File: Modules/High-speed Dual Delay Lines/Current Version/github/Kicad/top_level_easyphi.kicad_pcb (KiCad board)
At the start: 4 copper layers, 265 parts, among them J1 JTAG_CONNEC, J2 DM3D-SF(AS), P1 CONN_8, Q1 MOS_P, Q2 FDD8780, Q3 FDD8780, U1 MAX5924D, U10 2-1825027-0, U11 RLP1-600-800, U12 TE-5650478-5, U13 MAX9032AKA, U14 NB4L52, U15 TROU_FIX, U16 TROU_FIX, U17 RLP1-600-800, U18 RLP1-600-800, U19 RLP1-600-800, U2 MAX5925D, U20 RLP1-600-800, U21 RLP1-600-800, U22 CONNEC_QMA_ANO_2622-4035, U23 RLP1-600-800, U24 CONNEC_QMA_ANO_2622-4035, U25 CONNEC_QMA_ANO_2622-4035, U26 CONNEC_QMA_ANO_2622-4035, U27 CONNEC_QMA_ANO_2622-4035, U28 CONNEC_QMA_ANO_2622-4035, U29 NB6L11M, U3 24LC64, U30 SY89851U, U31 SY89297U, U32 MAX9032AKA, U33 NB4L52, U34 SY89851U, U35 NB6L11M, U36 AOZ1280, U4 USBLC6-2, U5 TPS7A4901, U51 CARD_BORDER, U52 CARD_BORDER, U53 CARD_BORDER, U54 CARD_BORDER, U6 AOZ1280, U7 SAM3X8E, U8 SN74LVC2G240DCTR, U9 SN65LVDM176DGK, X1 12MHz, X2 32.768KHz

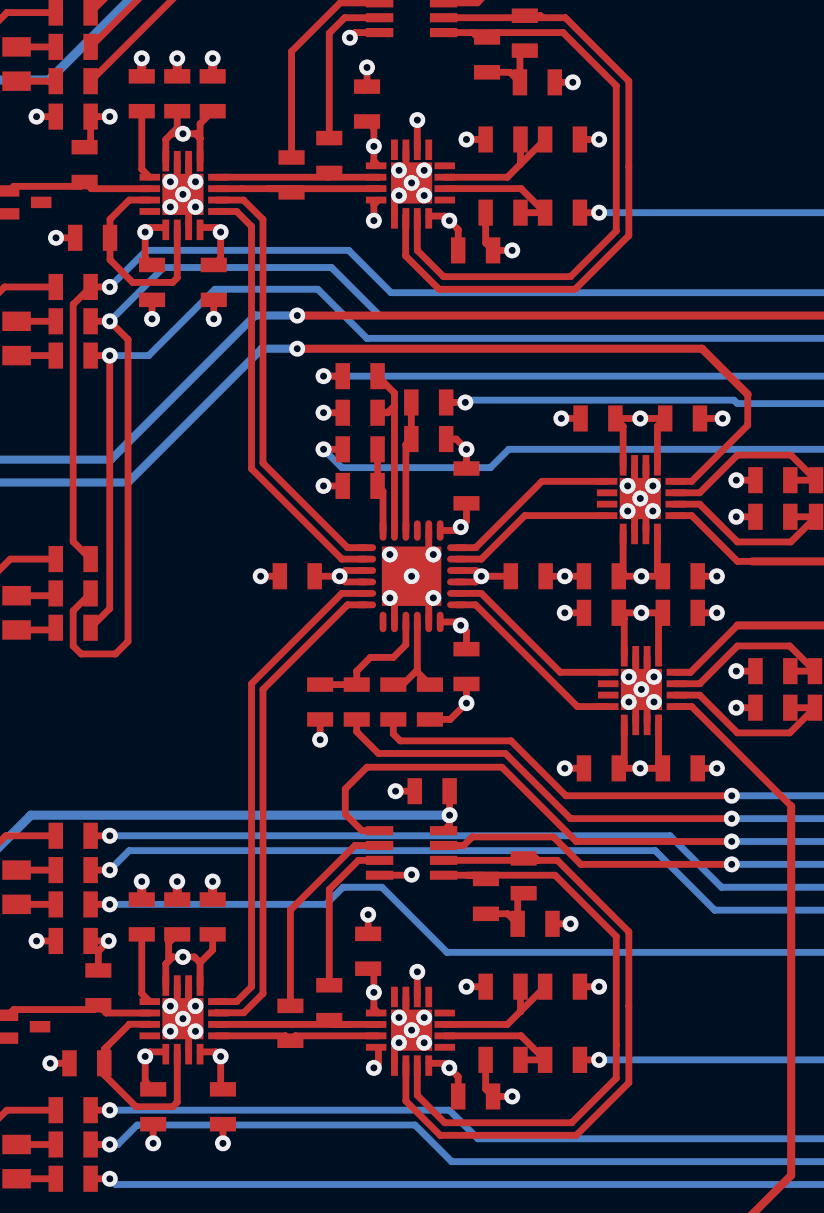
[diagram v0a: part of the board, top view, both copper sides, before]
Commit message: update delay lines
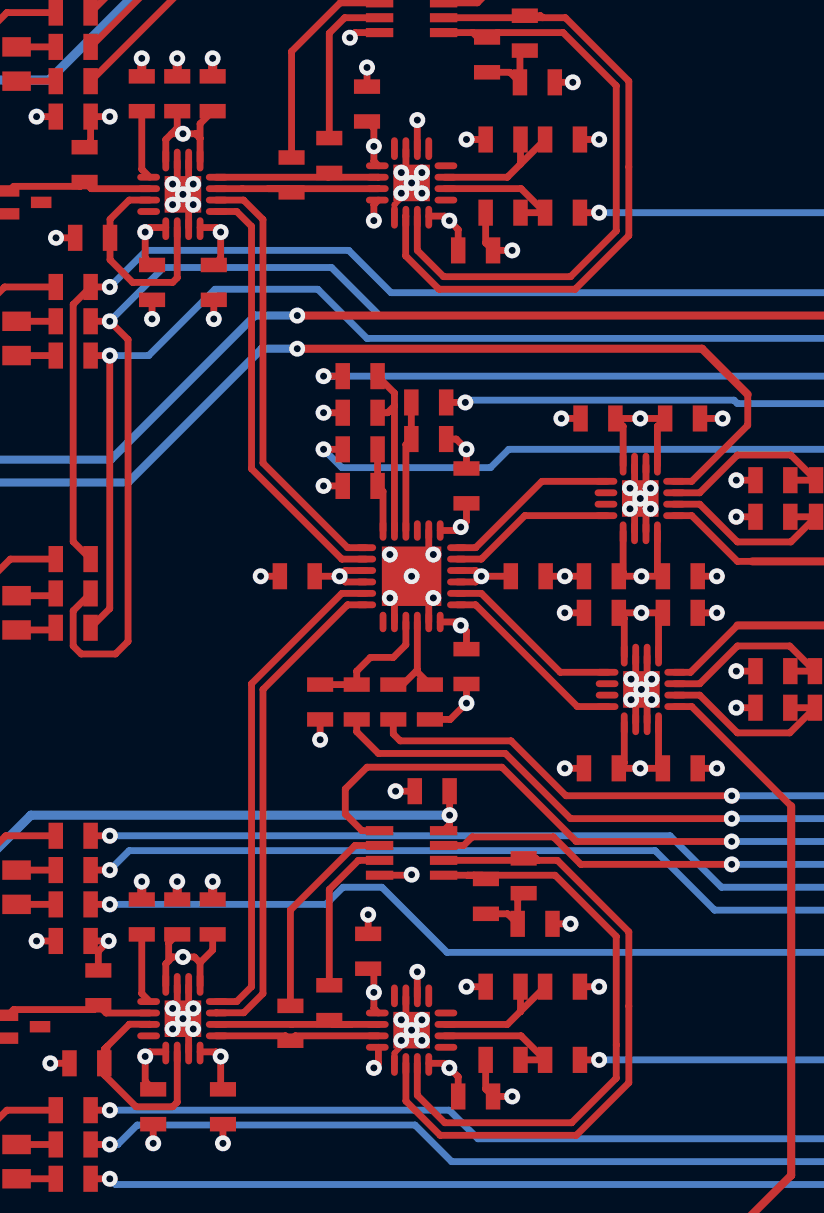
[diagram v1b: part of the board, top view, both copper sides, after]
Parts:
- U14, U29, U30, U33, U34, U35: footprint qfn16 -> QFN_16
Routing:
- net GND: track 634.4 -> 627.7 mm
